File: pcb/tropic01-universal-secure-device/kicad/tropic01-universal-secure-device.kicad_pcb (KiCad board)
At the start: 4 copper layers, 48 x 68 mm, 57 parts, among them J1 USB4105-GF-A, J2 54132-4062, J2B 52271-0679, J6 SM04B-SRSS-TB, J9 S2B-PH-SM4-TB, SW1 EVQP7J01P, SW2 EVQP7J01P, U1 STM32U585VIT6, U10 BQ24074RGTR, U11 OPTIGA-TRUST-M-SLS32AIA, U13 TPS22917DBVR, U15 TPS61165DBVR, U2 TR01-C2P-T301, U3 TPS62840DLCR, U4 TPS22917DBVR, U5 W25Q128JVSIQ, U6 TMUX1574RSVR, U7 TPD4E05U06DQAR, U8 TPS2553DBVR, U9 ST25R3916B-AQET, X1 16MHz, X3 FA-238 27.12MHz

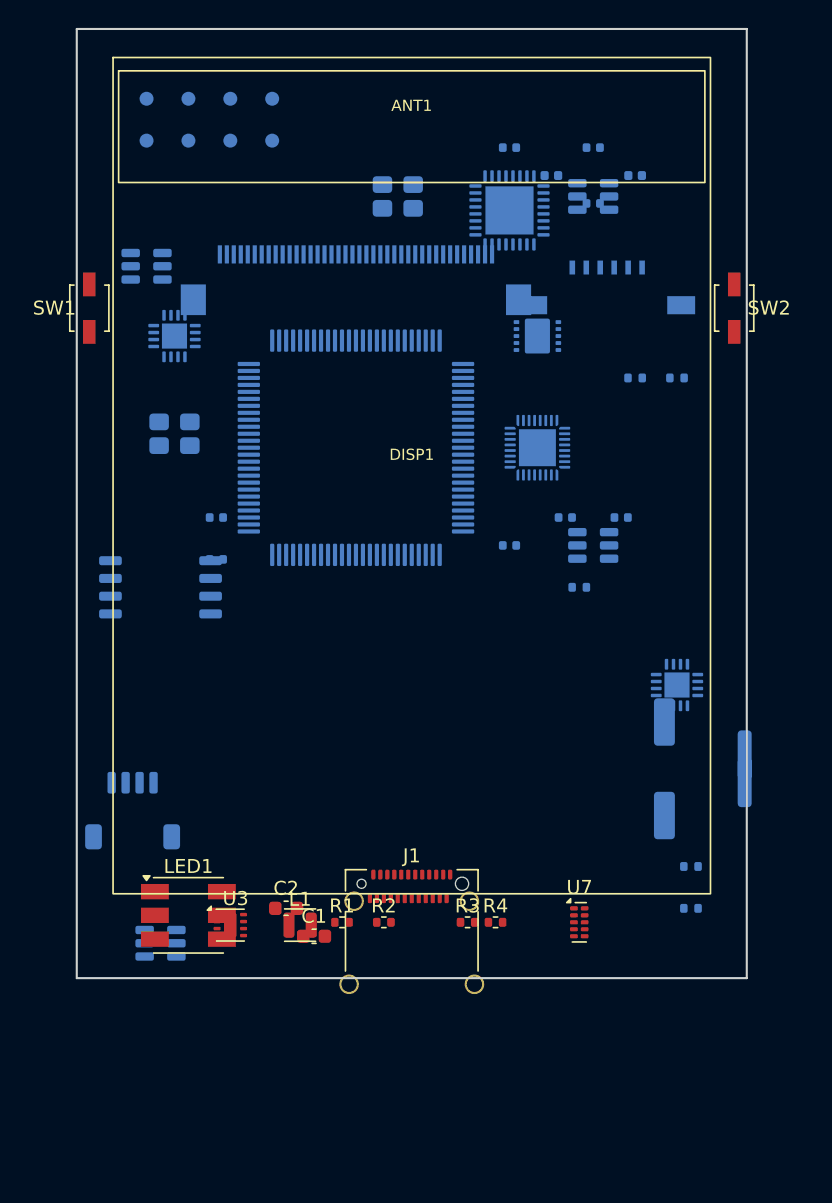
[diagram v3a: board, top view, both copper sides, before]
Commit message: hardware: adopt compact board B as base; automate display/battery/button changes
Adopt the user-confirmed compact board (two mounting holes, electronics on
the front, display on the back) as the base, replacing the regressed
worktree layout. Apply the agreed design changes headlessly via the KiCad
pcbnew Python module:

- Display: swap J2 to a single 50-pin 0.5mm FFC (Hirose FH12-50S-0.5SH) and
  remove the separate touch connector J2B; assign the display SPI + touch I2C
  nets to the new J2 pads.
- Battery: off-board in the enclosure; remove the on-board BAT1 envelope and
  keep only the J9 LiPo connector.
- Controls: single side button (SW1); drop SW2 across BOM, validator,
  schematic binding, schematic symbols, and placement (touch + one button).

Add the mechanical-architecture design note (display-sized device, PCB in the
lower portion, battery in the upper portion, back-side top-center NFC/RFID
antenna). Realign the test suite to board B; the two exact-coordinate
placement snapshots are skipped with a reason until the compact placement
pass re-establishes them.

make test: 79 pass (2 skipped); validate_hardware passes.
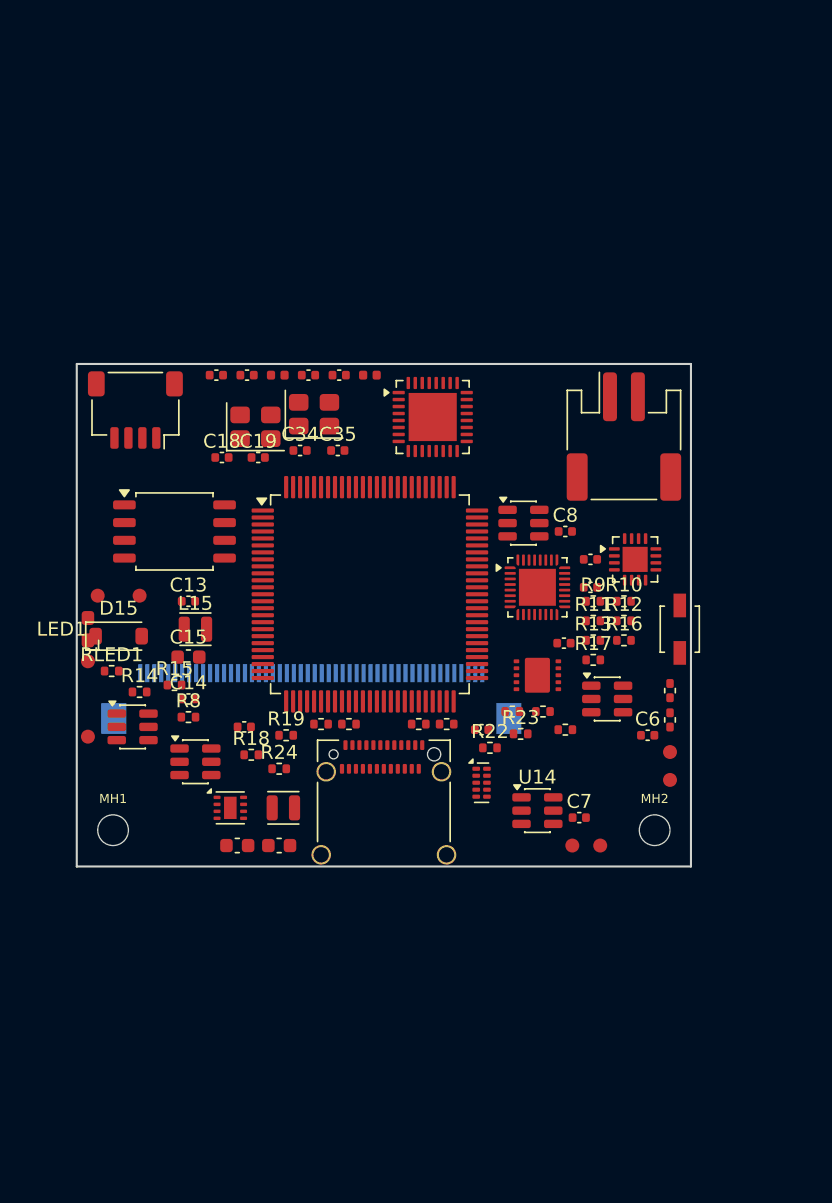
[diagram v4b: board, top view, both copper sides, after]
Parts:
- removed BAT1: LiPo_301020_REAR_ENVELOPE, nSealr_Mechanical:LiPo_301020_Rear_Envelope_30x20mm
- removed J2B: 52271-0679, Connector_FFC-FPC:Molex_52271-0679_1x06-1MP_P1.00mm_Horizontal
- removed SW2: EVQP7J01P, Button_Switch_SMD:SW_SPST_EVQP7C
- removed U6: TMUX1574RSVR, Package_DFN_QFN:VQFN-16-1EP_3x3mm_P0.5mm_EP1.8x1.8mm
- added C13: 220nF, Capacitor_SMD:C_0402_1005Metric, F.Cu at (18.0, 51.0)
- added C14: 1uF, Capacitor_SMD:C_0402_1005Metric, F.Cu at (18.0, 58.0)
- added C15: 1uF, Capacitor_SMD:C_0603_1608Metric, F.Cu at (18.0, 55.0)
- added C18: HSE_LOAD, Capacitor_SMD:C_0402_1005Metric, F.Cu at (20.4, 40.7)
- added C19: HSE_LOAD, Capacitor_SMD:C_0402_1005Metric, F.Cu at (23.0, 40.7)
- added C34: NFC_XTAL_LOAD, Capacitor_SMD:C_0402_1005Metric, F.Cu at (26.0, 40.2)
- added C35: NFC_XTAL_LOAD, Capacitor_SMD:C_0402_1005Metric, F.Cu at (28.7, 40.2)
- added C6: 1nF, Capacitor_SMD:C_0402_1005Metric, F.Cu at (50.9, 60.6)
- added C7: 1nF, Capacitor_SMD:C_0402_1005Metric, F.Cu at (46.0, 66.5)
- added C8: 1nF, Capacitor_SMD:C_0402_1005Metric, F.Cu at (45.0, 46.0)
- added D15: D_SCHOTTKY, Diode_SMD:D_SOD-123, F.Cu at (13.0, 53.5)
- added L15: 10uH, Inductor_SMD:L_Wuerth_PMFI-201610_PMCI-compatible, F.Cu at (18.5, 53.0)
- added MH1: M2_CASE_SCREW_CLEARANCE, nSealr_Mechanical:MountingHole_M2_Clearance_NPTH, F.Cu at (12.6, 67.4)
- added MH2: M2_CASE_SCREW_CLEARANCE, nSealr_Mechanical:MountingHole_M2_Clearance_NPTH, F.Cu at (51.4, 67.4)
- added R10: 1.13k, Resistor_SMD:R_0402_1005Metric, F.Cu at (49.2, 51.0)
- added R11: 46.4k, Resistor_SMD:R_0402_1005Metric, F.Cu at (47.0, 52.4)
- added R12: 4.12k, Resistor_SMD:R_0402_1005Metric, F.Cu at (49.2, 52.4)
- added R13: 10k, Resistor_SMD:R_0402_1005Metric, F.Cu at (47.0, 53.8)
- added R14: 100k, Resistor_SMD:R_0402_1005Metric, F.Cu at (14.5, 57.5)
- added R15: BL_SENSE, Resistor_SMD:R_0402_1005Metric, F.Cu at (17.0, 57.0)
- added R16: 100k, Resistor_SMD:R_0402_1005Metric, F.Cu at (49.2, 53.8)
- added R17: 100k, Resistor_SMD:R_0402_1005Metric, F.Cu at (47.0, 55.2)
- added R18: 267k, Resistor_SMD:R_0402_1005Metric, F.Cu at (22.5, 62.0)
- added R19: 10k, Resistor_SMD:R_0402_1005Metric, F.Cu at (25.0, 60.6)
- added R22: 100k, Resistor_SMD:R_0402_1005Metric, F.Cu at (39.6, 61.5)
- added R23: 100k, Resistor_SMD:R_0402_1005Metric, F.Cu at (41.8, 60.5)
- added R24: 1M, Resistor_SMD:R_0402_1005Metric, F.Cu at (24.5, 63.0)
- added R8: 27k, Resistor_SMD:R_0402_1005Metric, F.Cu at (18.0, 59.3)
- added R9: 1.18k, Resistor_SMD:R_0402_1005Metric, F.Cu at (47.0, 51.0)
- added RLED1: 1k, Resistor_SMD:R_0402_1005Metric, F.Cu at (12.5, 56.0)
- added U14: TPS22917DBVR, Package_TO_SOT_SMD:SOT-23-6, F.Cu at (43.0, 66.0)
- C16, C17, C3, C30, C31, C32, C33, C4, C5, J6, J9, L30, L31, R20, R21, R5, R6, R7, TP_3V3, TP_BOOT0, TP_GND, TP_NRST, TP_SWCLK, TP_SWDIO, TP_UART_RX, TP_UART_TX, U1, U11, U13, U15, U2, U4, U5, U8, U9, X1, X3: moved to F.Cu
- DISP1: moved to B.Cu
- J2: value 54132-4062 -> ER-TFT024IPS-3 50P FFC; footprint Connector_FFC-FPC:Molex_54132-4062_1x40-1MP_P0.50mm_Horizontal -> Hirose_FH12-50S-0.5SH_1x50-1MP_P0.50mm_Horizontal
- LED1: value APFA3010LSEEZGKQBKC -> APA1606SURCK; footprint LED_SMD:LED_RGB_5050-6 -> LED_SMD:LED_Kingbright_APA1606_1.6x0.6mm_Horizontal
- U10: footprint Package_DFN_QFN:VQFN-16-1EP_3.5x3.5mm_P0.5mm_EP2.1x2.1mm -> Package_DFN_QFN:VQFN-16-1EP_3x3mm_P0.5mm_EP1.6x1.6mm; moved to F.Cu
- U3: footprint Package_SON:WSON-8-1EP_2x2mm_P0.5mm_EP0.9x1.6mm -> Package_SON:Texas_VSON-HR-8_1.5x2mm_P0.5mm
- moved TP_UART_RX 58.5 mm to (47.5, 68.5)
- moved TP_BOOT0 57.7 mm to (45.5, 68.5)
- moved TP_3V3 54.0 mm to (52.5, 61.8)
- moved TP_GND 53.9 mm to (52.5, 63.8)
- moved SW1 48.1 mm to (53.2, 53.0)
- moved TP_UART_TX 42.9 mm to (10.8, 60.7)
- moved TP_NRST 41.6 mm to (10.8, 55.3)
- moved TP_SWCLK 35.8 mm to (14.5, 50.6)
- moved TP_SWDIO 35.8 mm to (11.5, 50.6)
- moved U15 33.0 mm to (14.0, 60.0)
- moved J2 30.2 mm to (26.8, 58.0), turned to 180 degrees
- moved C31 29.7 mm to (22.2, 34.8)
- moved J6 28.7 mm to (14.2, 37.3), turned to 180 degrees
- moved C30 26.6 mm to (20.0, 34.8)
- moved R7 25.8 mm to (43.4, 58.9)
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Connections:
- net BTN_LEFT renamed BTN_USER
- C1 pad 1: (no net) -> VBUS
- C1 pad 2: (no net) -> GND
- C16 pad 1: (no net) -> SYS_3V3
- C16 pad 2: (no net) -> GND
- C17 pad 1: (no net) -> SYS_3V3
- C17 pad 2: (no net) -> GND
- C2 pad 1: (no net) -> SYS_3V3
- C2 pad 2: (no net) -> GND
- C3 pad 1: (no net) -> TROPIC_VCC_SW
- C3 pad 2: (no net) -> GND
- C4 pad 1: (no net) -> TROPIC_VCC_SW
- C4 pad 2: (no net) -> GND
- C5 pad 1: (no net) -> TROPIC_VCC_SW
- C5 pad 2: (no net) -> GND
- J1 pad A6: USB_DP -> USB_DP_CONN
- J1 pad A7: USB_DM -> USB_DM_CONN
- J1 pad B6: USB_DP -> USB_DP_CONN
- J1 pad B7: USB_DM -> USB_DM_CONN
- J1 pad SH: (no net) -> GND
- J2 pad 1: GND -> TFT_BACKLIGHT_A
- J2 pad 10: TFT_CS -> TFT_RST
- J2 pad 11: TFT_DC -> (no net)
- J2 pad 12: TFT_SPI_SCK -> (no net)
- J2 pad 2: (no net) -> TFT_BACKLIGHT_K
- J2 pad 3: (no net) -> TFT_BACKLIGHT_K
- J2 pad 30: TFT_RST -> (no net)
- J2 pad 31: GND -> (no net)
- J2 pad 32: DISPLAY_VCC_SW -> (no net)
- J2 pad 33: DISPLAY_VCC_SW -> TFT_SPI_MISO
- J2 pad 34: TFT_BACKLIGHT_K -> TFT_SPI_MOSI
- J2 pad 35: TFT_BACKLIGHT_K -> (no net)
- J2 pad 36: TFT_BACKLIGHT_K -> TFT_DC
- J2 pad 37: TFT_BACKLIGHT_K -> TFT_SPI_SCK
- J2 pad 38: TFT_BACKLIGHT_A -> TFT_CS
- J2 pad 39: GND -> (no net)
- J2 pad 4: (no net) -> TFT_BACKLIGHT_K
- J2 pad 40: (no net) -> DISPLAY_VCC_SW
- J2 pad 5: (no net) -> TFT_BACKLIGHT_K
- J2 pad 6: (no net) -> GND
- J2 pad 9: TFT_SPI_MOSI -> DISPLAY_VCC_SW
- J6 pad 1: (no net) -> GND
- J6 pad 2: (no net) -> SYS_3V3
- J6 pad 3: (no net) -> EXP_I2C_SDA
- J6 pad 4: (no net) -> EXP_I2C_SCL
- L1 pad 1: (no net) -> BUCK_SW
- L1 pad 2: (no net) -> SYS_3V3
- LED1 pad 1: (no net) -> LED_STATUS_LED
- LED1 pad 2: (no net) -> GND
- R1 pad 1: (no net) -> USB_CC1_RD
- R1 pad 2: (no net) -> GND
- R2 pad 1: (no net) -> USB_CC2_RD
- R2 pad 2: (no net) -> GND
- R20 pad 1: (no net) -> VBAT
- R20 pad 2: (no net) -> VBAT_SENSE
- R21 pad 1: (no net) -> VBAT_SENSE
- R21 pad 2: (no net) -> GND
- R3 pad 1: (no net) -> USB_DP_CONN
- R3 pad 2: (no net) -> USB_DP
- R4 pad 1: (no net) -> USB_DM_CONN
- R4 pad 2: (no net) -> USB_DM
- R5 pad 1: (no net) -> TROPIC_PWR_EN
- R5 pad 2: (no net) -> GND
- R6 pad 1: (no net) -> SYS_3V3
- R6 pad 2: (no net) -> SE2_I2C_SCL
- R7 pad 1: (no net) -> SYS_3V3
- R7 pad 2: (no net) -> SE2_I2C_SDA
- U1 pad 10: (no net) -> GND
- U1 pad 100: (no net) -> SYS_3V3
- U1 pad 11: (no net) -> SYS_3V3
- U1 pad 12: (no net) -> HSE_IN
- U1 pad 13: (no net) -> HSE_OUT
- U1 pad 15: (no net) -> VBAT_SENSE
- U1 pad 19: (no net) -> GND
- U1 pad 2: BTN_RIGHT -> LED_STATUS
- U1 pad 20: (no net) -> GND
- U1 pad 21: (no net) -> SYS_3V3
- U1 pad 22: (no net) -> SYS_3V3
- U1 pad 28: (no net) -> SYS_3V3
- U1 pad 47: (no net) -> EXP_I2C_SCL
- U1 pad 48: (no net) -> EXP_I2C_SDA
- U1 pad 50: (no net) -> SYS_3V3
- U1 pad 6: (no net) -> SYS_3V3
- U1 pad 73: (no net) -> SYS_3V3
- U1 pad 75: (no net) -> SYS_3V3
- U10 pad 1: (no net) -> BAT_TS_FIXED
- U10 pad 10: (no net) -> SYS_PWR_IN
- U10 pad 11: (no net) -> SYS_PWR_IN
- U10 pad 12: (no net) -> CHARGER_ILIM
- U10 pad 13: (no net) -> VBUS_LIMITED
- U10 pad 14: (no net) -> CHARGER_TMR
- U10 pad 15: (no net) -> CHARGER_ITERM
- U10 pad 16: (no net) -> CHARGER_ISET
- U10 pad 17: (no net) -> GND
- U10 pad 2: (no net) -> VBAT
- U10 pad 3: (no net) -> VBAT
- U10 pad 4: (no net) -> GND
- U10 pad 5: (no net) -> SYS_PWR_IN
- U10 pad 6: (no net) -> GND
- U10 pad 7: (no net) -> CHARGER_PGOOD_N
- U10 pad 8: (no net) -> GND
- U10 pad 9: (no net) -> CHARGER_CHG_N
- U13 pad 1: (no net) -> SYS_3V3
- U13 pad 2: (no net) -> GND
- U13 pad 3: (no net) -> NFC_PWR_EN
- U13 pad 4: (no net) -> NFC_SW_CT
- U13 pad 5: (no net) -> NFC_VCC_SW
- U13 pad 6: (no net) -> NFC_VCC_SW
- U15 pad 1: (no net) -> SYS_PWR_IN
- U15 pad 2: (no net) -> TFT_BACKLIGHT_PWM
- U15 pad 3: (no net) -> TFT_BL_SW
- U15 pad 4: (no net) -> GND
- U15 pad 5: (no net) -> TFT_BL_COMP
- U15 pad 6: (no net) -> TFT_BACKLIGHT_K
- U2 pad 10: (no net) -> GND
- U2 pad 22: (no net) -> TROPIC_VCC_SW
- U2 pad 3: (no net) -> GND
- U2 pad 30: (no net) -> GND
- U2 pad 31: (no net) -> GND
- U2 pad 33: (no net) -> GND
- U2 pad 9: (no net) -> GND
- U3 pad 1: (no net) -> GND
- U3 pad 2: (no net) -> SYS_PWR_IN
- U3 pad 3: (no net) -> GND
- U3 pad 4: (no net) -> SYS_PWR_IN
- U3 pad 5: (no net) -> BUCK_VSET_3V3
- U3 pad 6: (no net) -> GND
- U3 pad 7: (no net) -> BUCK_SW
- U3 pad 8: (no net) -> SYS_3V3
- U4 pad 1: (no net) -> SYS_3V3
- U4 pad 2: (no net) -> GND
- U4 pad 3: (no net) -> TROPIC_PWR_EN
- U4 pad 4: (no net) -> TROPIC_SW_CT
- U4 pad 5: (no net) -> TROPIC_VCC_SW
- U4 pad 6: (no net) -> TROPIC_VCC_SW
- U7 pad 1: (no net) -> USB_DP_CONN
- U7 pad 2: (no net) -> USB_DM_CONN
- U7 pad 3: (no net) -> GND
- U7 pad 4: (no net) -> USB_CC1_RD
- U7 pad 5: (no net) -> USB_CC2_RD
- U7 pad 8: (no net) -> GND
- U8 pad 1: (no net) -> VBUS
- U8 pad 2: (no net) -> GND
- U8 pad 3: (no net) -> VBUS
- U8 pad 4: (no net) -> USB_FAULT_N
- U8 pad 5: (no net) -> USB_ILIM
- U8 pad 6: (no net) -> VBUS_LIMITED
- U9 pad 4: (no net) -> NFC_XTO
- U9 pad 5: (no net) -> NFC_XTI
- X1 pad 1: (no net) -> HSE_IN
- X1 pad 2: (no net) -> GND
- X1 pad 3: (no net) -> HSE_OUT
- X1 pad 4: (no net) -> GND
- X3 pad 1: (no net) -> NFC_XTO
- X3 pad 2: (no net) -> GND
- X3 pad 3: (no net) -> NFC_XTI
- X3 pad 4: (no net) -> GND
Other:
- board size 48 x 68 mm -> 44 x 36 mm
- board text removed: "ANT1 TOP EDGE NFC ANTENNA FPC OR TUNED KEEP-OUT"
- board text removed: "BOTTOM USB-C RECEPTACLE + POWER"
- board text removed: "CORE SILICON ZONE - STM32U5 + TROPIC01 + QSPI"
- board text removed: "DISP1 PORTRAIT TOUCH DISPLAY ENVELOPE 42.8 x 59.91 mm"
- board text removed: "EXT TROPIC SPI HOST"
- board text removed: "LEFT SIDE BUTTON"
- board text removed: "RIGHT SIDE BUTTON"
- board text removed: "TOP NFC / ANTENNA KEEP-OUT - no planes or tall metal"
- board text removed: "TROPIC01 restricted secure island"

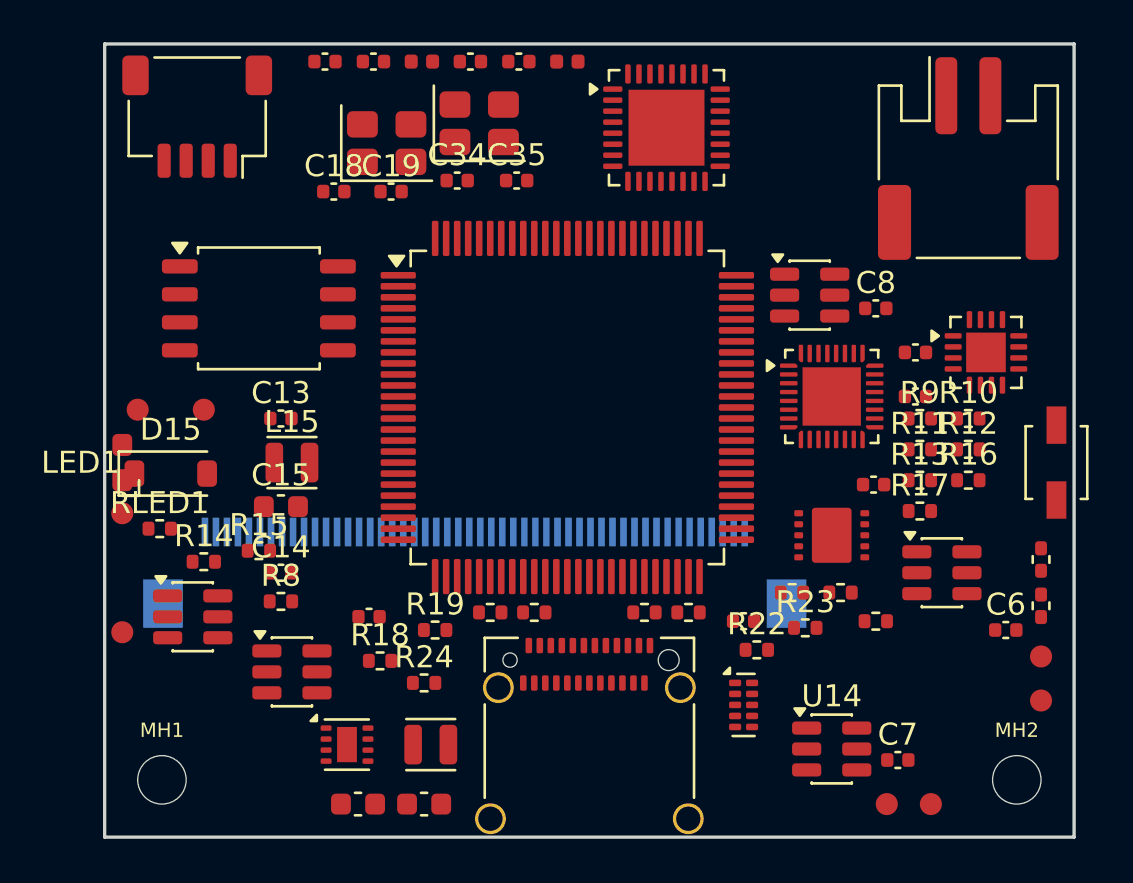
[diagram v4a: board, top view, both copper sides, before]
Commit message: hardware: cut DRC from 145 to 23 (placement/rules cleanup, automated)
Via pcbnew + project rules:
- Move the new 50-pin display FFC J2 up to clear the USB-C J1 mounting holes
  (removes the holes-in-courtyard violations).
- Hide reference designators on small passives (R/C/L/D); assembly uses the
  position file, so this clears most silk-over-copper and silk-overlap.
- Set copper-to-edge clearance to a manufacturable 0.2 mm (the USB-C, side
  button, and NFC matching network are intentional edge parts).
- Treat lib_footprint_mismatch / lib_footprint_issues as ignore (library-sync
  warnings; the board footprints are authoritative for fab).

Remaining 23 are two tight component clusters that need visual GUI placement
(LED1/D15 status-LED corner; X1 16 MHz crystal + load caps) plus cosmetic
silk/text. ERC stays 212 (schematic is still a scaffold; NFC RF front-end
undesigned). 246 nets remain unrouted.
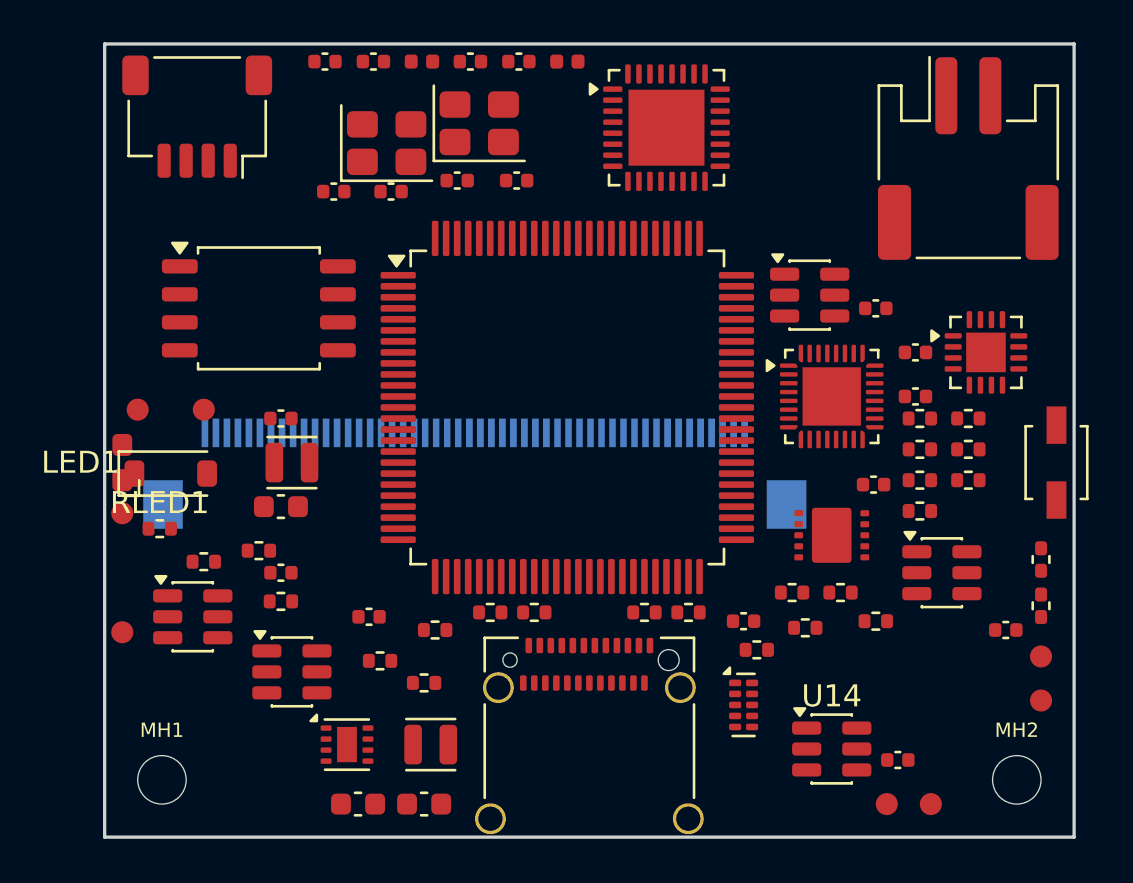
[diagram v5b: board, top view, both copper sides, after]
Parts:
- moved J2 4.50 mm to (26.8, 53.5)
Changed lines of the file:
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@@
 			(at 0 -1.17 0)
 			(layer "F.SilkS")
+			(hide yes)
 			(effects
 				(font
@@
 			(at 0 -1.17 0)
 			(layer "F.SilkS")
+			(hide yes)
 			(effects
 				(font
@@
 			(at 0 -1.17 0)
 			(layer "F.SilkS")
+			(hide yes)
 			(effects
 				(font
@@
 			(at 0 -1.16 0)
 			(layer "F.SilkS")
+			(hide yes)
 			(effects
 				(font
@@
 			(at 0 -1.43 0)
 			(layer "F.SilkS")
+			(hide yes)
 			(effects
 				(font
@@
 			(at 0 -1.17 0)
 			(layer "F.SilkS")
+			(hide yes)
 			(effects
 				(font
@@
 			(at 0 -1.85 0)
 			(layer "F.SilkS")
+			(hide yes)
 			(effects
 				(font
@@
 			(at 0 -1.16 0)
 			(layer "F.SilkS")
+			(hide yes)
 			(effects
 				(font
@@
 			(at 0 -1.17 0)
 			(layer "F.SilkS")
+			(hide yes)
 			(effects
 				(font
@@
 			(at 0 -1.17 0)
 			(layer "F.SilkS")
+			(hide yes)
 			(effects
 				(font
@@
 			(at 0 -1.17 0)
 			(layer "F.SilkS")
+			(hide yes)
 			(effects
 				(font
@@
 			(at 0 -1.17 0)
 			(layer "F.SilkS")
+			(hide yes)
 			(effects
 				(font
@@
 			(at 0 -1.17 0)
 			(layer "F.SilkS")
+			(hide yes)
 			(effects
 				(font
@@
 			(at 0 -1.17 0)
 			(layer "F.SilkS")
+			(hide yes)
 			(effects
 				(font
@@
 			(at 0 -1.16 0)
 			(layer "F.SilkS")
+			(hide yes)
 			(effects
 				(font
@@
 			(at 0 -1.17 0)
 			(layer "F.SilkS")
+			(hide yes)
 			(effects
 				(font
@@
 			(at 0 -1.17 0)
 			(layer "F.SilkS")
+			(hide yes)
 			(effects
 				(font
@@
 			(at 0 -1.17 0)
 			(layer "F.SilkS")
+			(hide yes)
 			(effects
 				(font
@@
 			(at 0 -1.16 0)
 			(layer "F.SilkS")
+			(hide yes)
 			(effects
 				(font
@@
 			(at 0 -2 0)
 			(layer "F.SilkS")
+			(hide yes)
 			(effects
 				(font
@@
 			(at 0 -1.17 0)
 			(layer "F.SilkS")
+			(hide yes)
 			(effects
 				(font
@@
 			(at 0 -1.16 0)
 			(layer "F.SilkS")
+			(hide yes)
 			(effects
 				(font
@@
 			(at 0 -1.16 0)
 			(layer "F.SilkS")
+			(hide yes)
 			(effects
 				(font
@@
 			(at 0 -1.16 0)
 			(layer "F.SilkS")
+			(hide yes)
 			(effects
 				(font
@@
 			(at 0 -1.16 0)
 			(layer "F.SilkS")
+			(hide yes)
 			(effects
 				(font
@@
 			(at 0 -1.17 0)
 			(layer "F.SilkS")
+			(hide yes)
 			(effects
 				(font
@@
 			(at 0 -1.16 0)
 			(layer "F.SilkS")
+			(hide yes)
 			(effects
 				(font
@@
 	(footprint "Hirose_FH12-50S-0.5SH_1x50-1MP_P0.50mm_Horizontal"
 		(layer "B.Cu")
-		(at 26.8 58 180)
+		(at 26.8 53.5 180)
 		(descr "Hirose FH12, FFC/FPC connector, FH12-50S-0.5SH, 50 Pins per row (https://www.hirose.com/product/en/products/FH12/FH12-24S-0.5SH(55)/)")
 		(tags "connector Hirose FH12 horizontal")
